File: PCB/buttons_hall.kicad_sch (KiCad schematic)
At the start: 18 parts, among them U1 ADC108S022CIMTX/NOPB, U10 DRV5053VAQDBZR, U11 DRV5053VAQDBZR, U12 DRV5053VAQDBZR, U13 DRV5053VAQDBZR, U14 DRV5053VAQDBZR, U15 DRV5053VAQDBZR, U16 DRV5053VAQDBZR, U17 DRV5053VAQDBZR, U18 DRV5053VAQDBZR, U19 DRV5053VAQDBZR, U3 ADC108S022CIMTX/NOPB, U4 DRV5053VAQDBZR, U5 DRV5053VAQDBZR, U6 DRV5053VAQDBZR, U7 DRV5053VAQDBZR, U8 DRV5053VAQDBZR, U9 DRV5053VAQDBZR

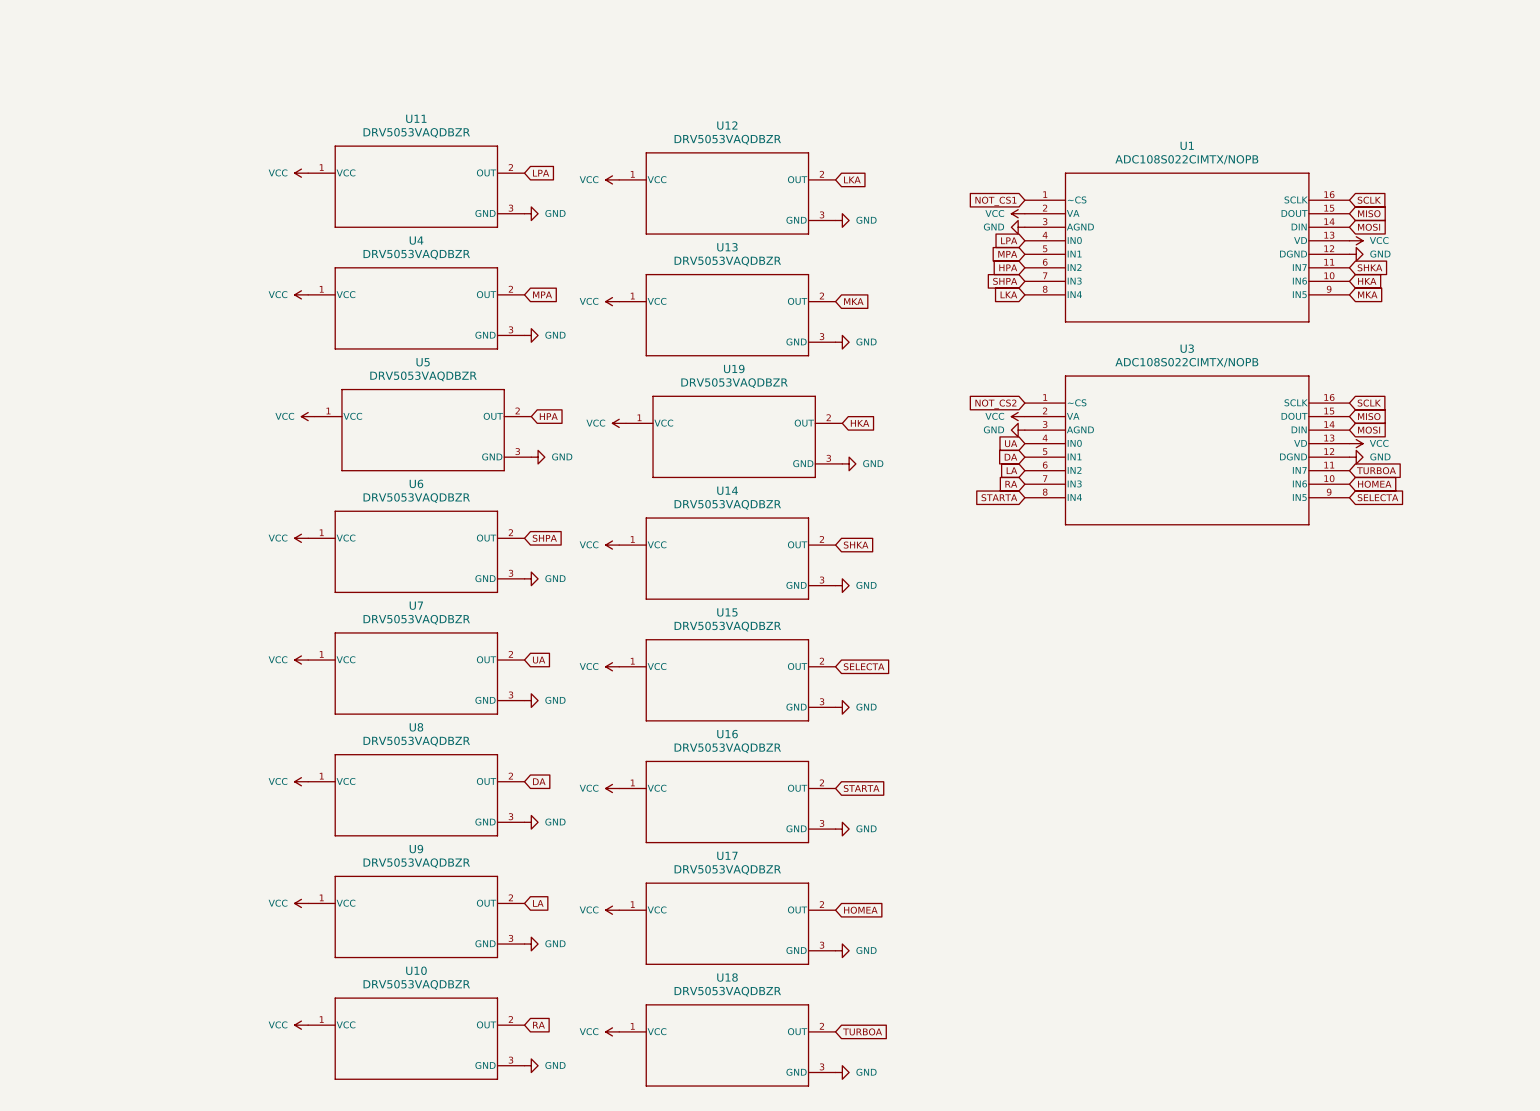
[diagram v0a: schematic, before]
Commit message: Updated PCB and schematic with the Gateron footprint, added dummy Brooks footprint
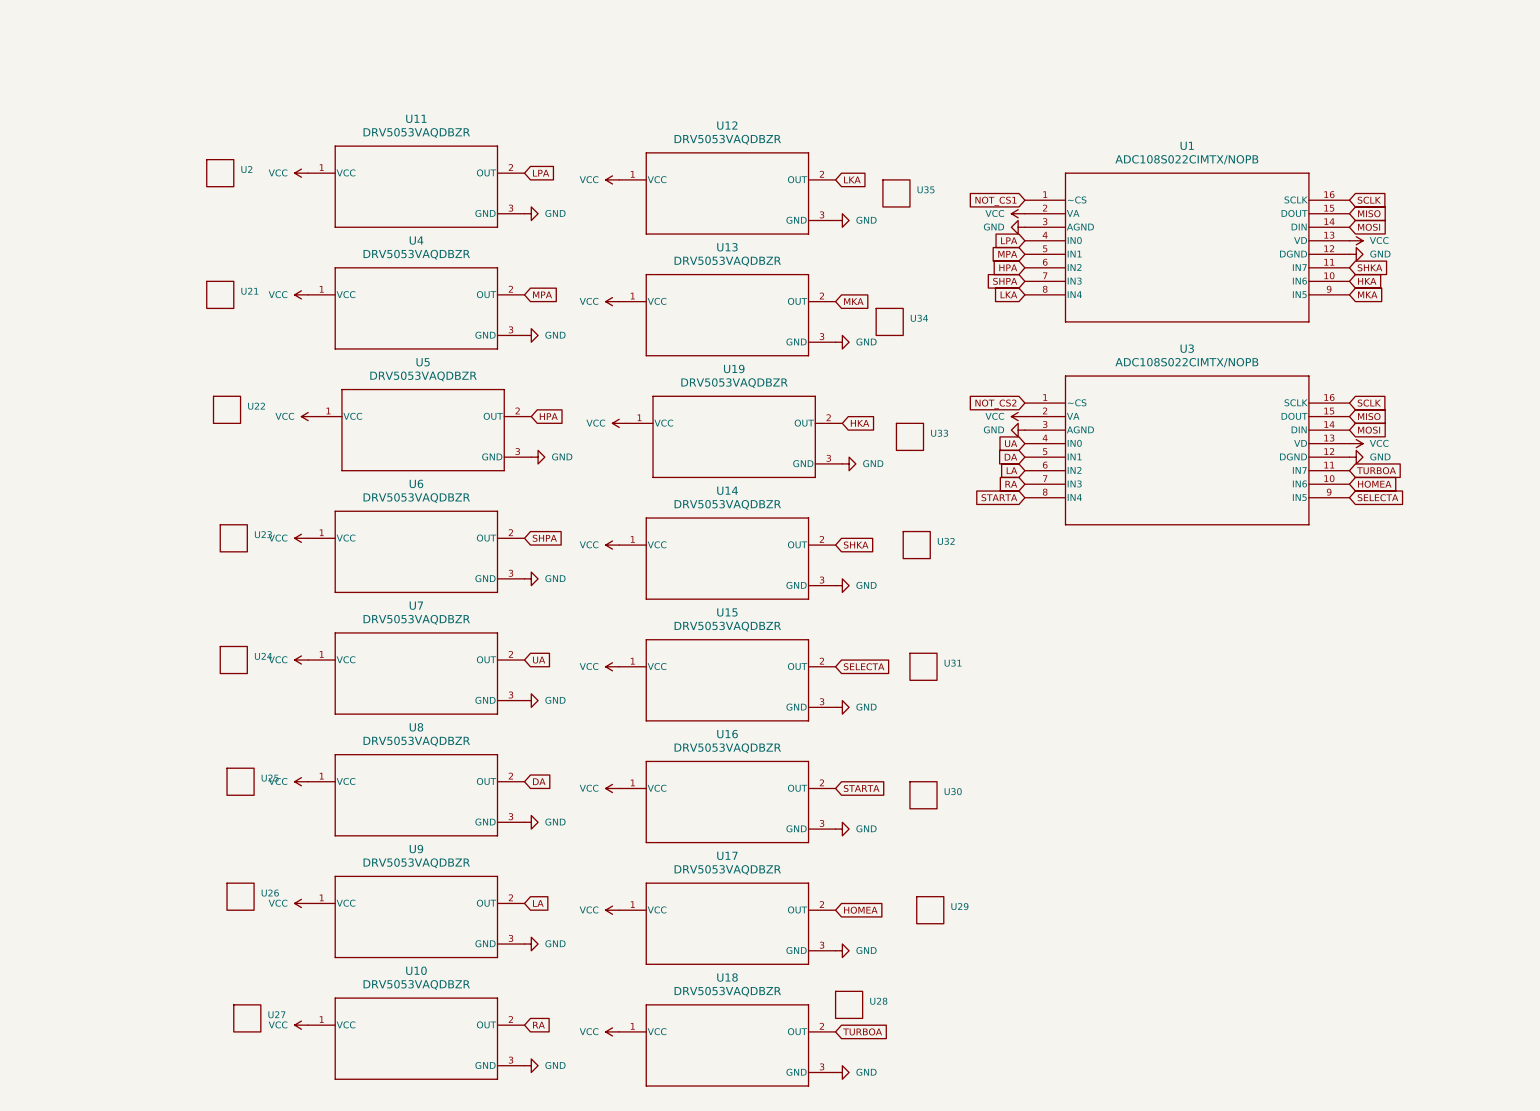
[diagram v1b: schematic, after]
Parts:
- added U2, U21, U22, U23, U24, U25, U26, U27, U28, U29, U30, U31, U32, U33, U34, U35: ~, key-switches:Gateron Jade Pro Magnetic, symbol KeyboardKeys:Gateron_Jade_Pro_Magnetic

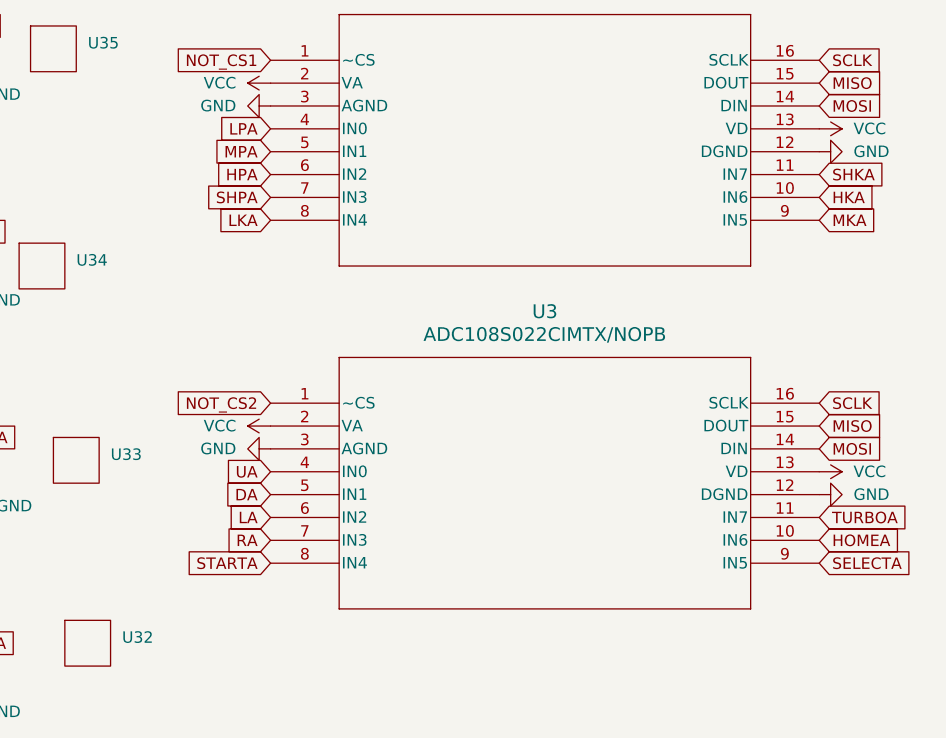
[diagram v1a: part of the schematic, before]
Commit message: Fallback Pico GP2040-CE added
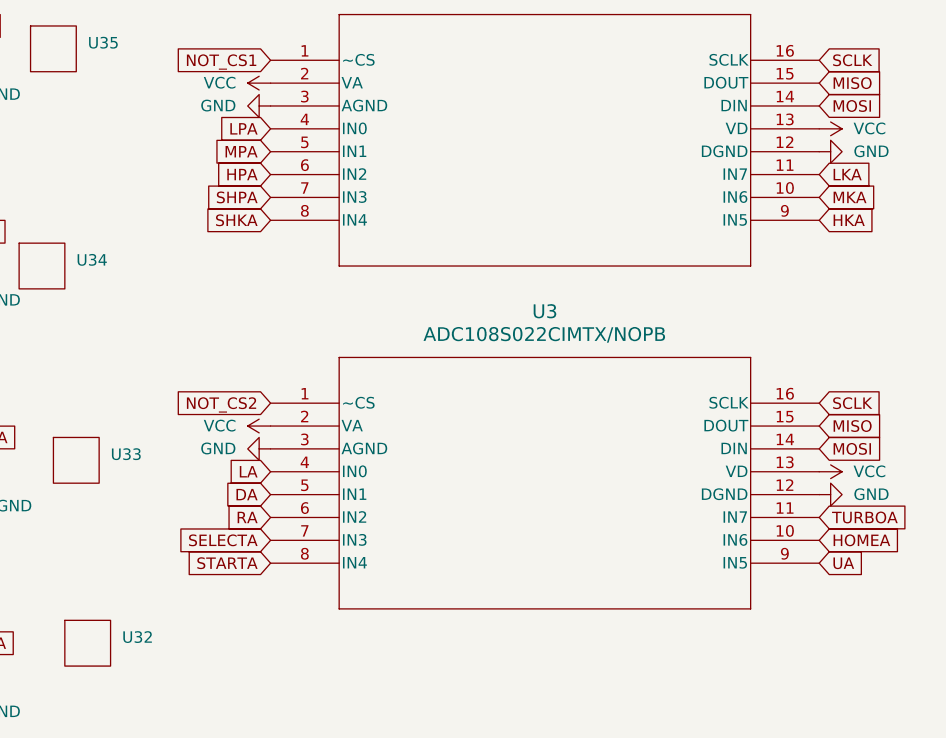
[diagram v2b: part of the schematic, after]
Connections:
- net HKA: now also U1.9 (IN5); no longer U1.10 (IN6)
- net LA: now also U3.4 (IN0); no longer U3.6 (IN2)
- net LKA: now also U1.11 (IN7); no longer U1.8 (IN4)
- net MKA: now also U1.10 (IN6); no longer U1.9 (IN5)
- net RA: now also U3.6 (IN2); no longer U3.7 (IN3)
- net SELECTA: now also U3.7 (IN3); no longer U3.9 (IN5)
- net SHKA: now also U1.8 (IN4); no longer U1.11 (IN7)
- net UA: now also U3.9 (IN5); no longer U3.4 (IN0)

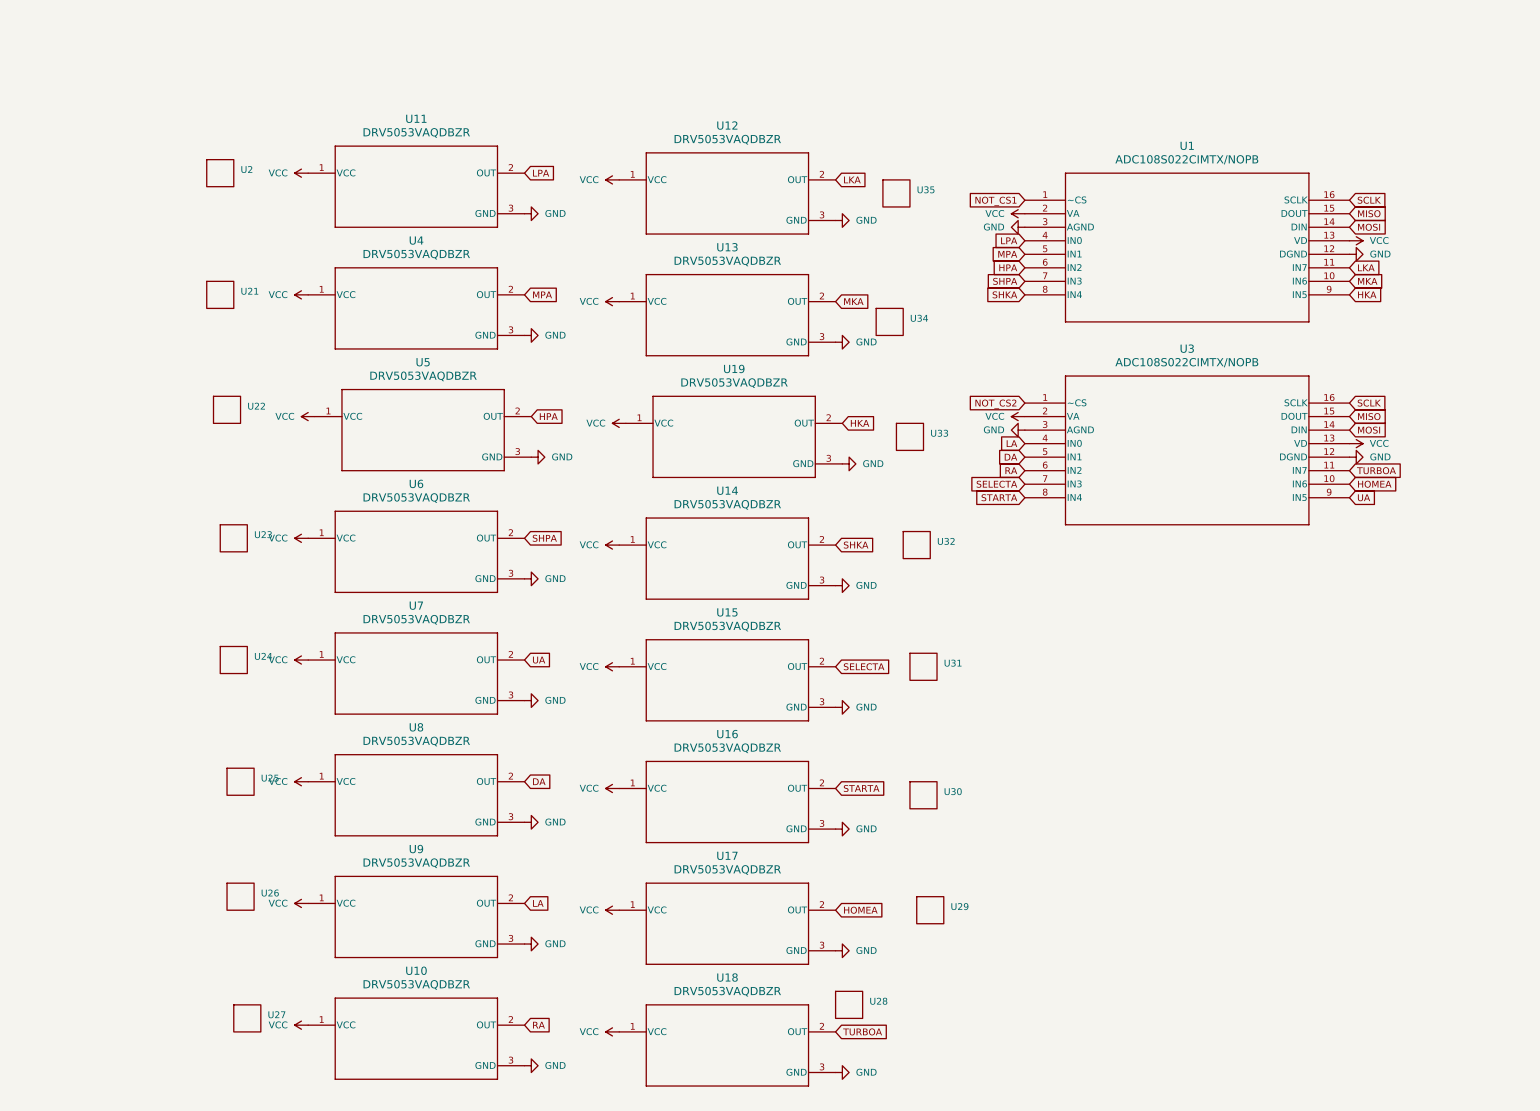
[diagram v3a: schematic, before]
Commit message: Added the additional components to support the ADCs
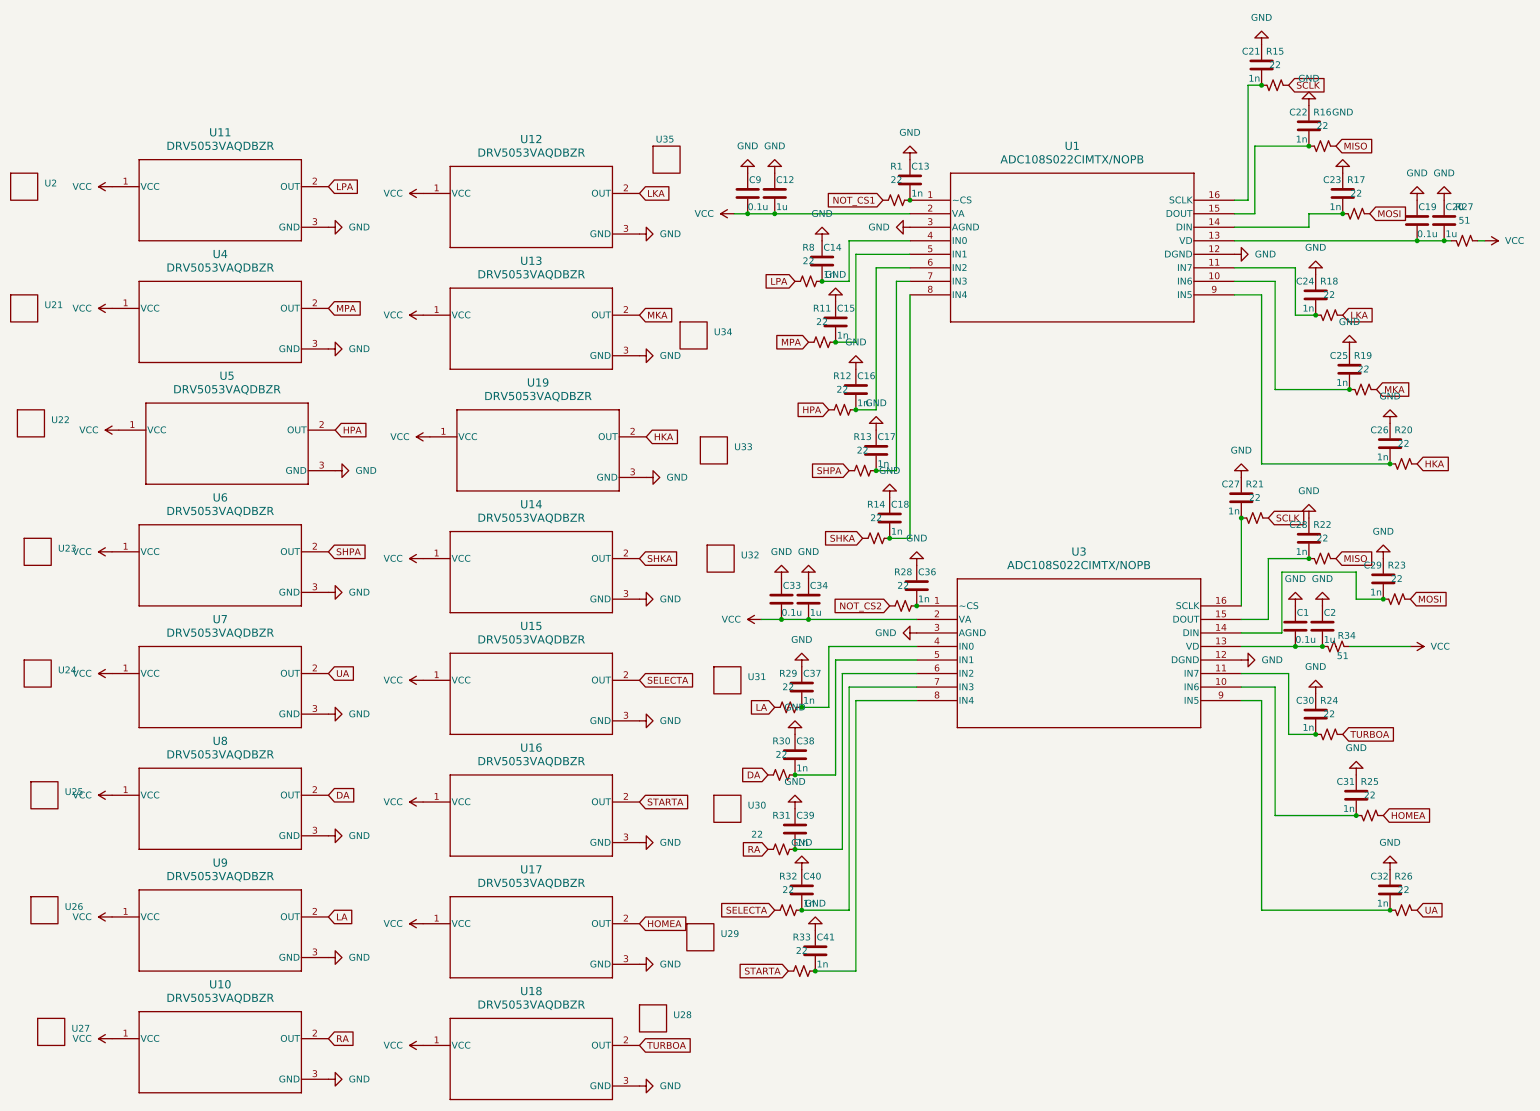
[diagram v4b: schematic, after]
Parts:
- added C1, C19, C33, C9: 0.1u, Capacitor_SMD:C_0603_1608Metric, symbol Device:C
- added C12, C2, C20, C34: 1u, Capacitor_SMD:C_0603_1608Metric, symbol Device:C
- added C13, C14, C15, C16, C17, C18, C21, C22, C23, C24, C25, C26, C27, C28, C29, C30, C31, C32, C36, C37, C38, C39, C40, C41: 1n, Capacitor_SMD:C_0603_1608Metric, symbol Device:C
- added R1, R11, R12, R13, R14, R15, R16, R17, R18, R19, R20, R21, R22, R23, R24, R25, R26, R28, R29, R30, R31, R32, R33, R8: 22, Resistor_SMD:R_0603_1608Metric, symbol Device:R_Small_US
- added R27, R34: 51, Resistor_SMD:R_0603_1608Metric, symbol Device:R_Small_US
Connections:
- net DA: now also R30.1; no longer U3.5 (IN1)
- net GND: now also C1.1, C12.1, C13.1, C14.1, C15.1, C16.1, C17.1, C18.1, C19.1, C2.1, C20.1, C21.1, C22.1, C23.1, C24.1, C25.1, C26.1, C27.1, C28.1, C29.1, C30.1, C31.1, C32.1, C33.1, C34.1, C36.1, C37.1, C38.1, C39.1, C40.1, C41.1, C9.1
- net HKA: now also R20.1; no longer U1.9 (IN5)
- net HOMEA: now also R25.1; no longer U3.10 (IN6)
- net HPA: now also R12.1; no longer U1.6 (IN2)
- net LA: now also R29.1; no longer U3.4 (IN0)
- net LKA: now also R18.1; no longer U1.11 (IN7)
- net LPA: now also R8.1; no longer U1.4 (IN0)
- net MISO: now also R16.1, R22.1; no longer U1.15 (DOUT), U3.15 (DOUT)
- net MKA: now also R19.1; no longer U1.10 (IN6)
- net MOSI: now also R17.1, R23.1; no longer U1.14 (DIN), U3.14 (DIN)
- net MPA: now also R11.1; no longer U1.5 (IN1)
- net NOT_CS1: now also R1.1; no longer U1.1 (~CS)
- net NOT_CS2: now also R28.1; no longer U3.1 (~CS)
- net RA: now also R31.1; no longer U3.6 (IN2)
- net SCLK: now also R15.1, R21.1; no longer U1.16 (SCLK), U3.16 (SCLK)
- net SELECTA: now also R32.1; no longer U3.7 (IN3)
- net SHKA: now also R14.1; no longer U1.8 (IN4)
- net SHPA: now also R13.1; no longer U1.7 (IN3)
- net STARTA: now also R33.1; no longer U3.8 (IN4)
- net TURBOA: now also R24.1; no longer U3.11 (IN7)
- net UA: now also R26.1; no longer U3.9 (IN5)
- net VCC: now also C12.2, C33.2, C34.2, C9.2, R27.1, R34.1; no longer U1.13 (VD), U3.13 (VD)
- new net: C38.2, R30.2, U3.5 (IN1)
- new net: C15.2, R11.2, U1.5 (IN1)
- new net: C17.2, R13.2, U1.7 (IN3)
- new net: C21.2, R15.2, U1.16 (SCLK)
- new net: C22.2, R16.2, U1.15 (DOUT)
- new net: C29.2, R23.2, U3.14 (DIN)
- new net: C39.2, R31.2, U3.6 (IN2)
- new net: C26.2, R20.2, U1.9 (IN5)
- new net: C1.2, C2.2, R34.2, U3.13 (VD)
- new net: C41.2, R33.2, U3.8 (IN4)
- new net: C19.2, C20.2, R27.2, U1.13 (VD)
- new net: C31.2, R25.2, U3.10 (IN6)
- new net: C30.2, R24.2, U3.11 (IN7)
- new net: C36.2, R28.2, U3.1 (~CS)
- new net: C32.2, R26.2, U3.9 (IN5)
- new net: C23.2, R17.2, U1.14 (DIN)
- new net: C40.2, R32.2, U3.7 (IN3)
- new net: C25.2, R19.2, U1.10 (IN6)
- new net: C37.2, R29.2, U3.4 (IN0)
- new net: C13.2, R1.2, U1.1 (~CS)
- new net: C28.2, R22.2, U3.15 (DOUT)
- new net: C18.2, R14.2, U1.8 (IN4)
- new net: C16.2, R12.2, U1.6 (IN2)
- new net: C27.2, R21.2, U3.16 (SCLK)
- new net: C24.2, R18.2, U1.11 (IN7)
- new net: C14.2, R8.2, U1.4 (IN0)
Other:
- moved on the sheet: U1, U10, U11, U12, U13, U14, U15, U16, U17, U18, U19, U2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
